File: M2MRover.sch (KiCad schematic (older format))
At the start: 10 parts, among them J1 Light Detection, J2 Serial (Bluetooth), J3 Servo, J4 H-Bridge, J5 Ultrasonic Down, J6 Ultrasonic Forward, J7 Compass GY-273, J8 Left Hall, J9 Right Hall

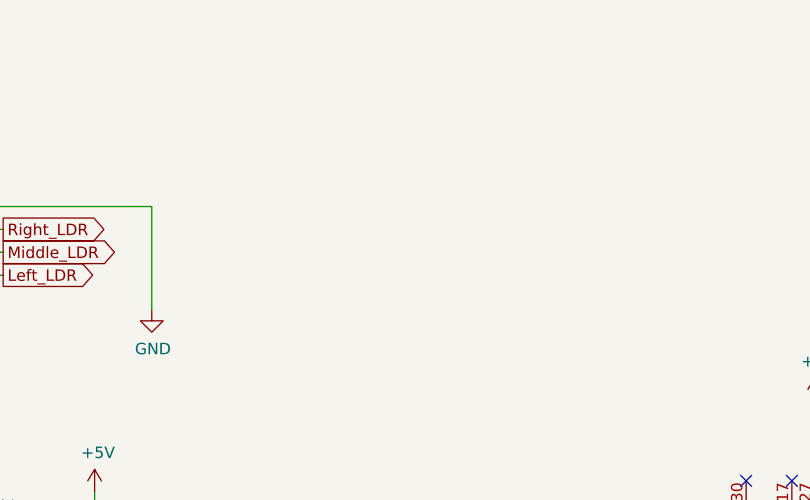
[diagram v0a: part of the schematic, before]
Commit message: Add Gyroscope & Accelerometer
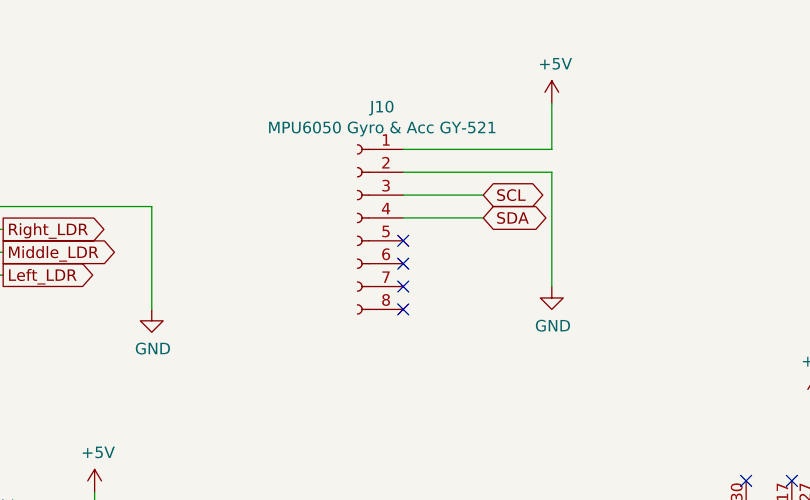
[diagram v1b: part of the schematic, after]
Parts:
- added J10: MPU6050 Gyro & Acc GY-521, Connector_PinSocket_2.54mm:PinSocket_1x08_P2.54mm_Vertical, symbol Connector:Conn_01x08_Female
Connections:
- net +5V: now also J10.1 (Pin_1)
- net GND: now also J10.2 (Pin_2)
- net SCL: now also J10.3 (Pin_3)
- net SDA: now also J10.4 (Pin_4)
- no-connect marks 5 -> 9
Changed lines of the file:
@@
 NoConn ~ 5700 2750
 NoConn ~ 5900 2750
+$Comp
+L Connector:Conn_01x08_Female J10
+U 1 1 5D5A6131
+P 4000 1600
+F 0 "J10" H 3892 2085 50  0000 C CNN
+F 1 "MPU6050 Gyro & Acc GY-521" H 3892 1994 50  0000 C CNN
+F 2 "Connector_PinSocket_2.54mm:PinSocket_1x08_P2.54mm_Vertical" H 4000 1600 50  0001 C CNN
+F 3 "~" H 4000 1600 50  0001 C CNN
+	1    4000 1600
+	-1   0    0    -1
+$EndComp
+$Comp
+L power:+5V #PWR01
+U 1 1 5D5ABD9B
+P 4850 1100
+F 0 "#PWR01" H 4850 950 50  0001 C CNN
+F 1 "+5V" H 4865 1273 50  0000 C CNN
+F 2 "" H 4850 1100 50  0001 C CNN
+F 3 "" H 4850 1100 50  0001 C CNN
+	1    4850 1100
+	1    0    0    -1
+$EndComp
+$Comp
+L power:GND #PWR02
+U 1 1 5D5AC5FF
+P 4850 1900
+F 0 "#PWR02" H 4850 1650 50  0001 C CNN
+F 1 "GND" H 4855 1727 50  0000 C CNN
+F 2 "" H 4850 1900 50  0001 C CNN
+F 3 "" H 4850 1900 50  0001 C CNN
+	1    4850 1900
+	1    0    0    -1
+$EndComp
+Text GLabel 4550 1500 2    50   BiDi ~ 0
+SCL
+Text GLabel 4550 1600 2    50   BiDi ~ 0
+SDA
+Wire Wire Line
+	4200 1300 4850 1300
+Wire Wire Line
+	4850 1300 4850 1100
+Wire Wire Line
+	4200 1400 4850 1400
+Wire Wire Line
+	4850 1400 4850 1900
+Wire Wire Line
+	4550 1500 4200 1500
+Wire Wire Line
+	4200 1600 4550 1600
+NoConn ~ 4200 1700
+NoConn ~ 4200 1800
+NoConn ~ 4200 1900
+NoConn ~ 4200 2000
 $EndSCHEMATC
